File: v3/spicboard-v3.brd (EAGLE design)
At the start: 65 x 60 mm, 40 parts, among them IC1 74HC595, Q1 BC557, Q2 BC557

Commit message: SPiCboard: Bauteile aus Standard-Bibliotheken
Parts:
- BLUE0, BLUE1, GREEN0, GREEN1, RED0, RED1, YELLOW0, YELLOW1: device spicboard-v3:LED5MM -> led:LED5MM
- R1, R10, R11, R12, R13, R14, R15, R2, R3, R4, R5, R6, R7, R8, R9: device spicboard-v3:0207/10 -> resistor:0207/10
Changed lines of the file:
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@@
 <elements>
 <element name="B1" library="spicboard-v3" package="UNO_R3_SHIELD_FINAL" value="ARDUINO_UNO_R3_SHIELD" x="24.13" y="35.56"/>
-<element name="BLUE0" library="spicboard-v3" package="LED5MM" value="" x="4.1" y="33.7" smashed="yes">
+<element name="BLUE0" library="led" package="LED5MM" value="" x="4.1" y="33.7" smashed="yes">
 <attribute name="VALUE" x="7.3004" y="31.8966" size="1.27" layer="25" ratio="10"/>
 </element>
-<element name="BLUE1" library="spicboard-v3" package="LED5MM" value="" x="4.1" y="4.1" smashed="yes">
+<element name="BLUE1" library="led" package="LED5MM" value="" x="4.1" y="4.1" smashed="yes">
 <attribute name="VALUE" x="7.3004" y="2.2966" size="1.27" layer="25" ratio="10"/>
 </element>
-<element name="GREEN0" library="spicboard-v3" package="LED5MM" value="" x="4.1" y="41.1" smashed="yes">
+<element name="GREEN0" library="led" package="LED5MM" value="" x="4.1" y="41.1" smashed="yes">
 <attribute name="VALUE" x="7.3004" y="39.2966" size="1.27" layer="25" ratio="10"/>
 </element>
-<element name="GREEN1" library="spicboard-v3" package="LED5MM" value="" x="4.1" y="11.5" smashed="yes">
+<element name="GREEN1" library="led" package="LED5MM" value="" x="4.1" y="11.5" smashed="yes">
 <attribute name="VALUE" x="7.3004" y="9.6966" size="1.27" layer="25" ratio="10"/>
 </element>
-<element name="R1" library="spicboard-v3" package="0207/10" value="330" x="14.605" y="46.355" smashed="yes">
+<element name="R1" library="resistor" package="0207/10" value="330" x="14.605" y="46.355" smashed="yes">
 <attribute name="VALUE" x="12.3444" y="45.72" size="1.27" layer="25" ratio="10"/>
 </element>
-<element name="R2" library="spicboard-v3" package="0207/10" value="330" x="14.605" y="42.545" smashed="yes">
+<element name="R2" library="resistor" package="0207/10" value="330" x="14.605" y="42.545" smashed="yes">
 <attribute name="VALUE" x="12.3444" y="41.91" size="1.27" layer="25" ratio="10"/>
 </element>
-<element name="R3" library="spicboard-v3" package="0207/10" value="330" x="14.605" y="38.735" smashed="yes">
+<element name="R3" library="resistor" package="0207/10" value="330" x="14.605" y="38.735" smashed="yes">
 <attribute name="VALUE" x="12.3444" y="38.1" size="1.27" layer="25" ratio="10"/>
 </element>
-<element name="R4" library="spicboard-v3" package="0207/10" value="10k" x="14.605" y="34.925" smashed="yes">
+<element name="R4" library="resistor" package="0207/10" value="10k" x="14.605" y="34.925" smashed="yes">
 <attribute name="VALUE" x="12.3444" y="34.29" size="1.27" layer="25" ratio="10"/>
 </element>
-<element name="R5" library="spicboard-v3" package="0207/10" value="330" x="14.605" y="31.115" smashed="yes">
+<element name="R5" library="resistor" package="0207/10" value="330" x="14.605" y="31.115" smashed="yes">
 <attribute name="VALUE" x="12.3444" y="30.48" size="1.27" layer="25" ratio="10"/>
 </element>
-<element name="R6" library="spicboard-v3" package="0207/10" value="330" x="14.605" y="27.305" smashed="yes">
+<element name="R6" library="resistor" package="0207/10" value="330" x="14.605" y="27.305" smashed="yes">
 <attribute name="VALUE" x="12.3444" y="26.67" size="1.27" layer="25" ratio="10"/>
 </element>
-<element name="R7" library="spicboard-v3" package="0207/10" value="330" x="14.605" y="23.495" smashed="yes">
+<element name="R7" library="resistor" package="0207/10" value="330" x="14.605" y="23.495" smashed="yes">
 <attribute name="VALUE" x="12.3444" y="22.86" size="1.27" layer="25" ratio="10"/>
 </element>
-<element name="R8" library="spicboard-v3" package="0207/10" value="10k" x="14.605" y="19.685" smashed="yes">
+<element name="R8" library="resistor" package="0207/10" value="10k" x="14.605" y="19.685" smashed="yes">
 <attribute name="VALUE" x="12.3444" y="19.05" size="1.27" layer="25" ratio="10"/>
 </element>
-<element name="RED0" library="spicboard-v3" package="LED5MM" value="" x="4.1" y="55.9" smashed="yes">
+<element name="RED0" library="led" package="LED5MM" value="" x="4.1" y="55.9" smashed="yes">
 <attribute name="VALUE" x="7.3004" y="54.0966" size="1.27" layer="25" ratio="10"/>
 </element>
-<element name="RED1" library="spicboard-v3" package="LED5MM" value="" x="4.1" y="26.3" smashed="yes">
+<element name="RED1" library="led" package="LED5MM" value="" x="4.1" y="26.3" smashed="yes">
 <attribute name="VALUE" x="7.3004" y="24.4966" size="1.27" layer="25" ratio="10"/>
 </element>
-<element name="YELLOW0" library="spicboard-v3" package="LED5MM" value="" x="4.1" y="48.5" smashed="yes">
+<element name="YELLOW0" library="led" package="LED5MM" value="" x="4.1" y="48.5" smashed="yes">
 <attribute name="VALUE" x="7.3004" y="46.6966" size="1.27" layer="25" ratio="10"/>
 </element>
-<element name="YELLOW1" library="spicboard-v3" package="LED5MM" value="" x="4.1" y="18.9" smashed="yes">
+<element name="YELLOW1" library="led" package="LED5MM" value="" x="4.1" y="18.9" smashed="yes">
 <attribute name="VALUE" x="7.3004" y="17.0966" size="1.27" layer="25" ratio="10"/>
 </element>
@@
 <attribute name="MF" value="" x="41.275" y="19.685" size="1.778" layer="25" display="off"/>
 </element>
-<element name="R10" library="spicboard-v3" package="0207/10" value="49.9k" x="54.2925" y="36.195" smashed="yes" rot="R270">
+<element name="R10" library="resistor" package="0207/10" value="49.9k" x="54.2925" y="36.195" smashed="yes" rot="R270">
 <attribute name="VALUE" x="53.6575" y="38.4556" size="1.27" layer="25" ratio="10" rot="R270"/>
 </element>
-<element name="R9" library="spicboard-v3" package="0207/10" value="1k" x="23.495" y="36.195" smashed="yes" rot="R270">
+<element name="R9" library="resistor" package="0207/10" value="1k" x="23.495" y="36.195" smashed="yes" rot="R270">
 <attribute name="VALUE" x="24.13" y="33.9344" size="1.27" layer="25" ratio="10" rot="R90"/>
 </element>
-<element name="R11" library="spicboard-v3" package="0207/10" value="1k" x="26.67" y="36.195" smashed="yes" rot="R270">
+<element name="R11" library="resistor" package="0207/10" value="1k" x="26.67" y="36.195" smashed="yes" rot="R270">
 <attribute name="VALUE" x="27.305" y="33.9344" size="1.27" layer="25" ratio="10" rot="R90"/>
 </element>
@@
 <attribute name="VALUE" x="27.305" y="45.593" size="1.27" layer="25" ratio="10" align="bottom-center"/>
 </element>
-<element name="R12" library="spicboard-v3" package="0207/10" value="1k" x="46.355" y="2.54" smashed="yes">
+<element name="R12" library="resistor" package="0207/10" value="1k" x="46.355" y="2.54" smashed="yes">
 <attribute name="VALUE" x="44.0944" y="1.905" size="1.27" layer="25" ratio="10"/>
 </element>
@@
 <attribute name="VALUE" x="58.674" y="3.175" size="1.27" layer="25" ratio="10" align="top-left"/>
 </element>
-<element name="R13" library="spicboard-v3" package="0207/10" value="330" x="57.785" y="50.165" smashed="yes">
+<element name="R13" library="resistor" package="0207/10" value="330" x="57.785" y="50.165" smashed="yes">
 <attribute name="VALUE" x="55.5244" y="49.53" size="1.27" layer="25" ratio="10"/>
 </element>
-<element name="R14" library="spicboard-v3" package="0207/10" value="330" x="57.785" y="47.3075" smashed="yes">
+<element name="R14" library="resistor" package="0207/10" value="330" x="57.785" y="47.3075" smashed="yes">
 <attribute name="VALUE" x="55.5244" y="46.6725" size="1.27" layer="25" ratio="10"/>
 </element>
@@
 <attribute name="VALUE" x="55.88" y="55.753" size="0.6096" layer="25" font="vector" ratio="20"/>
 </element>
-<element name="R15" library="spicboard-v3" package="0207/10" value="1k" x="57.785" y="44.45" smashed="yes">
+<element name="R15" library="resistor" package="0207/10" value="1k" x="57.785" y="44.45" smashed="yes">
 <attribute name="VALUE" x="55.5244" y="43.815" size="1.27" layer="25" ratio="10"/>
 </element>
@@
 <wire x1="34.29" y1="57.785" x2="35.8775" y2="59.3725" width="0.4064" layer="16"/>
 <wire x1="35.8775" y1="59.3725" x2="45.4025" y2="59.3725" width="0.4064" layer="16"/>
-<wire x1="58.7375" y1="4.445" x2="60.0075" y2="5.715" width="0.4064" layer="1"/>
-<wire x1="60.0075" y1="5.715" x2="60.0075" y2="30.1625" width="0.4064" layer="1"/>
+<wire x1="58.42" y1="4.445" x2="59.69" y2="5.715" width="0.4064" layer="1"/>
+<wire x1="59.69" y1="5.715" x2="59.69" y2="30.48" width="0.4064" layer="1"/>
 <wire x1="63.1825" y1="59.3725" x2="64.389" y2="58.166" width="0.4064" layer="1"/>
 <wire x1="63.1825" y1="59.3725" x2="48.5775" y2="59.3725" width="0.4064" layer="1"/>
@@
 <wire x1="32.385" y1="48.895" x2="46.355" y2="48.895" width="0.4064" layer="1"/>
 <wire x1="24.13" y1="6.35" x2="26.035" y2="4.445" width="0.4064" layer="1"/>
-<wire x1="26.035" y1="4.445" x2="58.7375" y2="4.445" width="0.4064" layer="1"/>
+<wire x1="26.035" y1="4.445" x2="58.42" y2="4.445" width="0.4064" layer="1"/>
 <wire x1="32.385" y1="48.895" x2="31.75" y2="48.26" width="0.4064" layer="1"/>
 <wire x1="31.75" y1="48.26" x2="31.75" y2="46.99" width="0.4064" layer="1"/>
@@
 <wire x1="46.99" y1="48.26" x2="46.99" y2="46.99" width="0.4064" layer="1"/>
 <wire x1="46.99" y1="45.4025" x2="49.53" y2="42.8625" width="0.4064" layer="1"/>
-<wire x1="62.865" y1="33.02" x2="60.0075" y2="30.1625" width="0.4064" layer="1"/>
+<wire x1="62.865" y1="33.655" x2="59.69" y2="30.48" width="0.4064" layer="1"/>
 <contactref element="R15" pad="2"/>
 <wire x1="64.389" y1="45.974" x2="62.865" y2="44.45" width="0.4064" layer="1"/>
 <wire x1="64.389" y1="58.166" x2="64.389" y2="45.974" width="0.4064" layer="1"/>
-<wire x1="62.865" y1="44.45" x2="62.865" y2="33.02" width="0.4064" layer="1"/>
+<wire x1="62.865" y1="44.45" x2="62.865" y2="33.655" width="0.4064" layer="1"/>
 <wire x1="60.325" y1="37.465" x2="62.865" y2="40.005" width="0.4064" layer="16"/>
 <wire x1="62.865" y1="40.005" x2="62.865" y2="44.45" width="0.4064" layer="16"/>

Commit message: SPiCboard...
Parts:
- C1, C2: device spicboard-v3:C2.5-2 -> capacitor-wima:C2.5-2
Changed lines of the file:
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@@
 <attribute name="VALUE" x="27.305" y="33.9344" size="1.27" layer="25" ratio="10" rot="R90"/>
 </element>
-<element name="C1" library="spicboard-v3" package="C2.5-2" value="100n" x="27.305" y="44.069" smashed="yes" rot="R180">
+<element name="C1" library="capacitor-wima" package="C2.5-2" value="100n" x="27.305" y="44.069" smashed="yes" rot="R180">
 <attribute name="VALUE" x="27.305" y="45.593" size="1.27" layer="25" ratio="10" align="bottom-center"/>
 </element>
@@
 <attribute name="VALUE" x="44.0944" y="1.905" size="1.27" layer="25" ratio="10"/>
 </element>
-<element name="C2" library="spicboard-v3" package="C2.5-2" value="100n" x="55.88" y="2.54" smashed="yes" rot="R180">
+<element name="C2" library="capacitor-wima" package="C2.5-2" value="100n" x="55.88" y="2.54" smashed="yes" rot="R180">
 <attribute name="VALUE" x="58.674" y="3.175" size="1.27" layer="25" ratio="10" align="top-left"/>
 </element>

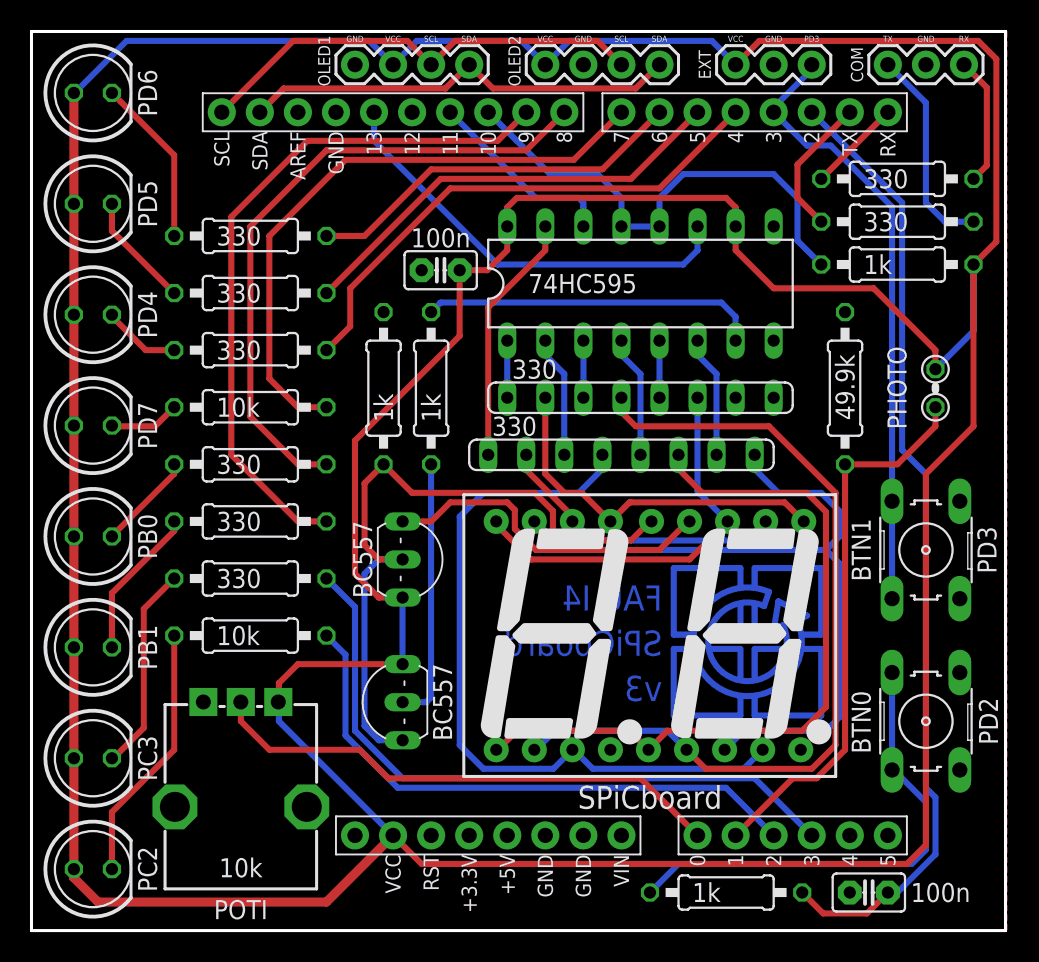
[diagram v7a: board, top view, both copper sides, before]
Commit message: SPiCboard: PADs fertig
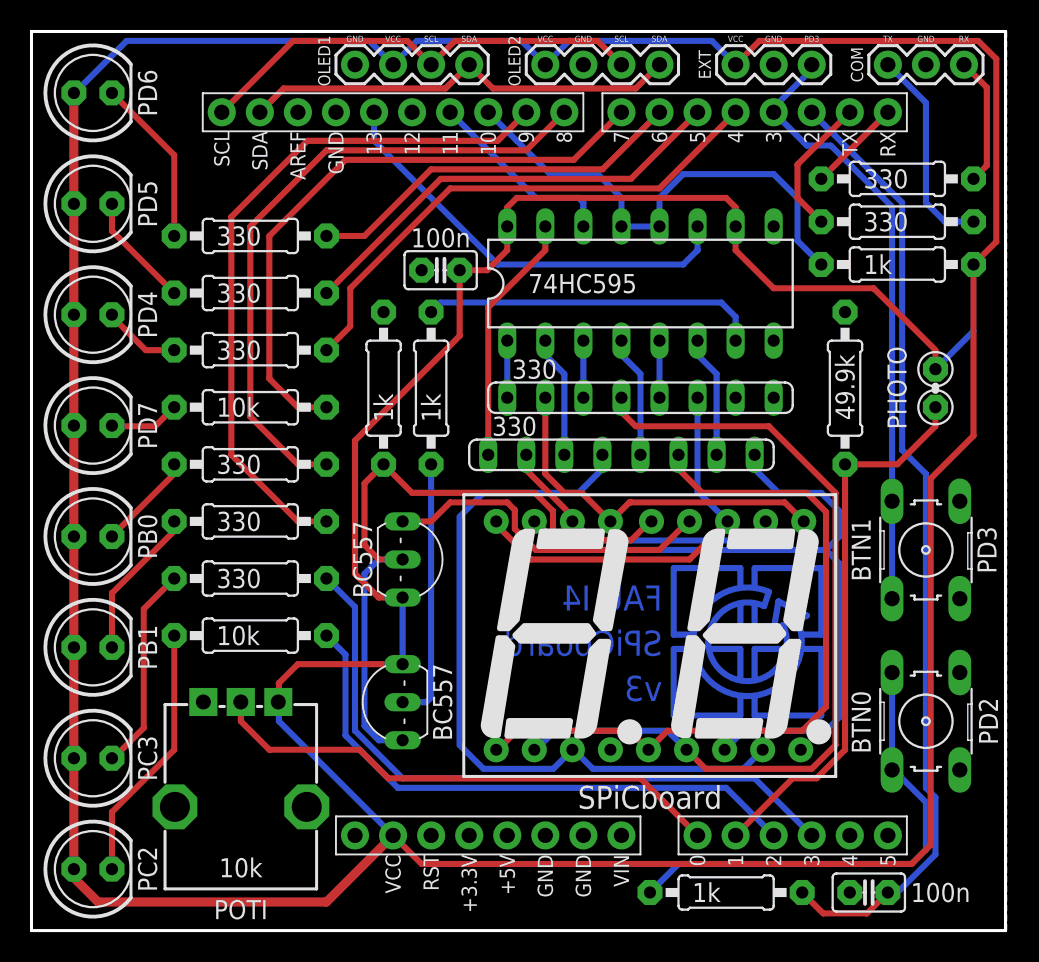
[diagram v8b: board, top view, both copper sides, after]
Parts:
- BLUE0, BLUE1, GREEN0, GREEN1, RED0, RED1, YELLOW0, YELLOW1: device led:LED5MM -> spicboard-v3:LED5MM
- C1, C2: device capacitor-wima:C2.5-2 -> spicboard-v3:C2.5-2
- R1, R10, R11, R12, R13, R14, R15, R2, R3, R4, R5, R6, R7, R8, R9: device resistor:0207/10 -> spicboard-v3:0207/10
